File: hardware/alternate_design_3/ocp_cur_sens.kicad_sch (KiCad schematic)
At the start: 23 parts, among them U2 INA181, U3 INA181, U4 INA181, U8 LMV321, U9 TL331

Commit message: updates to kicad schema
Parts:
- added R4: R, symbol Device:R
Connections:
- net SD_A: now also R4.2
- net SENS_A: now also U9.1 (-), R4.1
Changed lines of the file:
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@@
+	)
+	(junction
+		(at 228.6 101.6)
+		(diameter 0)
+		(color 0 0 0 0)
 	)
 	(junction
@@
 		(color 0 0 0 0)
 	)
+	(junction
+		(at 205.74 104.14)
+		(diameter 0)
+		(color 0 0 0 0)
+	)
 	(wire
 		(pts
@@
 	(wire
 		(pts
+			(xy 205.74 104.14) (xy 205.74 124.46)
+		)
+		(stroke
+			(width 0)
+			(type default)
+		)
+	)
+	(wire
+		(pts
 			(xy 25.4 129.54) (xy 29.21 129.54)
 		)
@@
 	(wire
 		(pts
+			(xy 228.6 101.6) (xy 228.6 124.46)
+		)
+		(stroke
+			(width 0)
+			(type default)
+		)
+	)
+	(wire
+		(pts
 			(xy 34.29 182.88) (xy 34.29 185.42)
 		)
@@
 	(wire
 		(pts
+			(xy 198.12 104.14) (xy 205.74 104.14)
+		)
+		(stroke
+			(width 0)
+			(type default)
+		)
+	)
+	(wire
+		(pts
 			(xy 34.29 69.85) (xy 34.29 81.28)
 		)
@@
 	(wire
 		(pts
+			(xy 228.6 101.6) (xy 238.76 101.6)
+		)
+		(stroke
+			(width 0)
+			(type default)
+		)
+	)
+	(wire
+		(pts
 			(xy 59.69 165.1) (xy 59.69 163.83)
 		)
@@
 	(wire
 		(pts
+			(xy 205.74 104.14) (xy 210.82 104.14)
+		)
+		(stroke
+			(width 0)
+			(type default)
+		)
+	)
+	(wire
+		(pts
 			(xy 125.73 168.91) (xy 125.73 161.29)
 		)
@@
 	(wire
 		(pts
-			(xy 226.06 101.6) (xy 238.76 101.6)
+			(xy 226.06 101.6) (xy 228.6 101.6)
+		)
+		(stroke
+			(width 0)
+			(type default)
+		)
+	)
+	(wire
+		(pts
+			(xy 205.74 124.46) (xy 212.09 124.46)
 		)
 		(stroke
@@
 		(pts
 			(xy 198.12 99.06) (xy 210.82 99.06)
+		)
+		(stroke
+			(width 0)
+			(type default)
+		)
+	)
+	(wire
+		(pts
+			(xy 219.71 124.46) (xy 228.6 124.46)
 		)
 		(stroke
@@
 			)
 			(justify left bottom)
+		)
+	)
+	(label "VSHUNT_A"
+		(at 198.12 104.14 180)
+		(effects
+			(font
+				(size 1.27 1.27)
+			)
+			(justify right bottom)
 		)
 	)
@@
 	)
 	(symbol
+		(lib_id "Device:R")
+		(at 215.9 124.46 90)
+		(unit 1)
+		(body_style 1)
+		(exclude_from_sim no)
+		(in_bom yes)
+		(on_board yes)
+		(in_pos_files yes)
+		(dnp no)
+		(property "Reference" "R4"
+			(at 215.9 122.174 90)
+			(show_name no)
+			(do_not_autoplace no)
+			(effects
+				(font
+					(size 1.27 1.27)
+				)
+			)
+		)
+		(property "Value" "R"
+			(at 215.9 127.254 90)
+			(show_name no)
+			(do_not_autoplace no)
+			(effects
+				(font
+					(size 1.27 1.27)
+				)
+			)
+		)
+		(property "Footprint" ""
+			(at 215.9 126.238 90)
+			(hide yes)
+			(show_name no)
+			(do_not_autoplace no)
+			(effects
+				(font
+					(size 1.27 1.27)
+				)
+			)
+		)
+		(property "Datasheet" ""
+			(at 215.9 124.46 0)
+			(hide yes)
+			(show_name no)
+			(do_not_autoplace no)
+			(effects
+				(font
+					(size 1.27 1.27)
+				)
+			)
+		)
+		(property "Description" "Resistor"
+			(at 215.9 124.46 0)
+			(hide yes)
+			(show_name no)
+			(do_not_autoplace no)
+			(effects
+				(font
+					(size 1.27 1.27)
+				)
+			)
+		)
+		(pin "1"
+		)
+		(pin "2"
+		)
+		(instances
+			(project "mosfets"
+				(path "/6b82a8a8-ae2c-4987-9dc0-17eac5149d3f/902fe731-fd21-46ba-b7ee-b1d6cec2ca3c"
+					(reference "R4")
+					(unit 1)
+				)
+			)
+		)
+	)
+	(symbol
 		(lib_id "power:GNDA")
 		(at 34.29 185.42 0)
@@
 		(in_pos_files yes)
 		(dnp no)
-		(fields_autoplaced yes)
 		(property "Reference" "#PWR047"
 			(at 215.9 120.65 0)
@@
 		)
 		(property "Value" "GNDA"
-			(at 215.9 119.38 0)
-			(show_name no)
-			(do_not_autoplace no)
+			(at 215.9 118.364 0)
+			(show_name no)
+			(do_not_autoplace no)

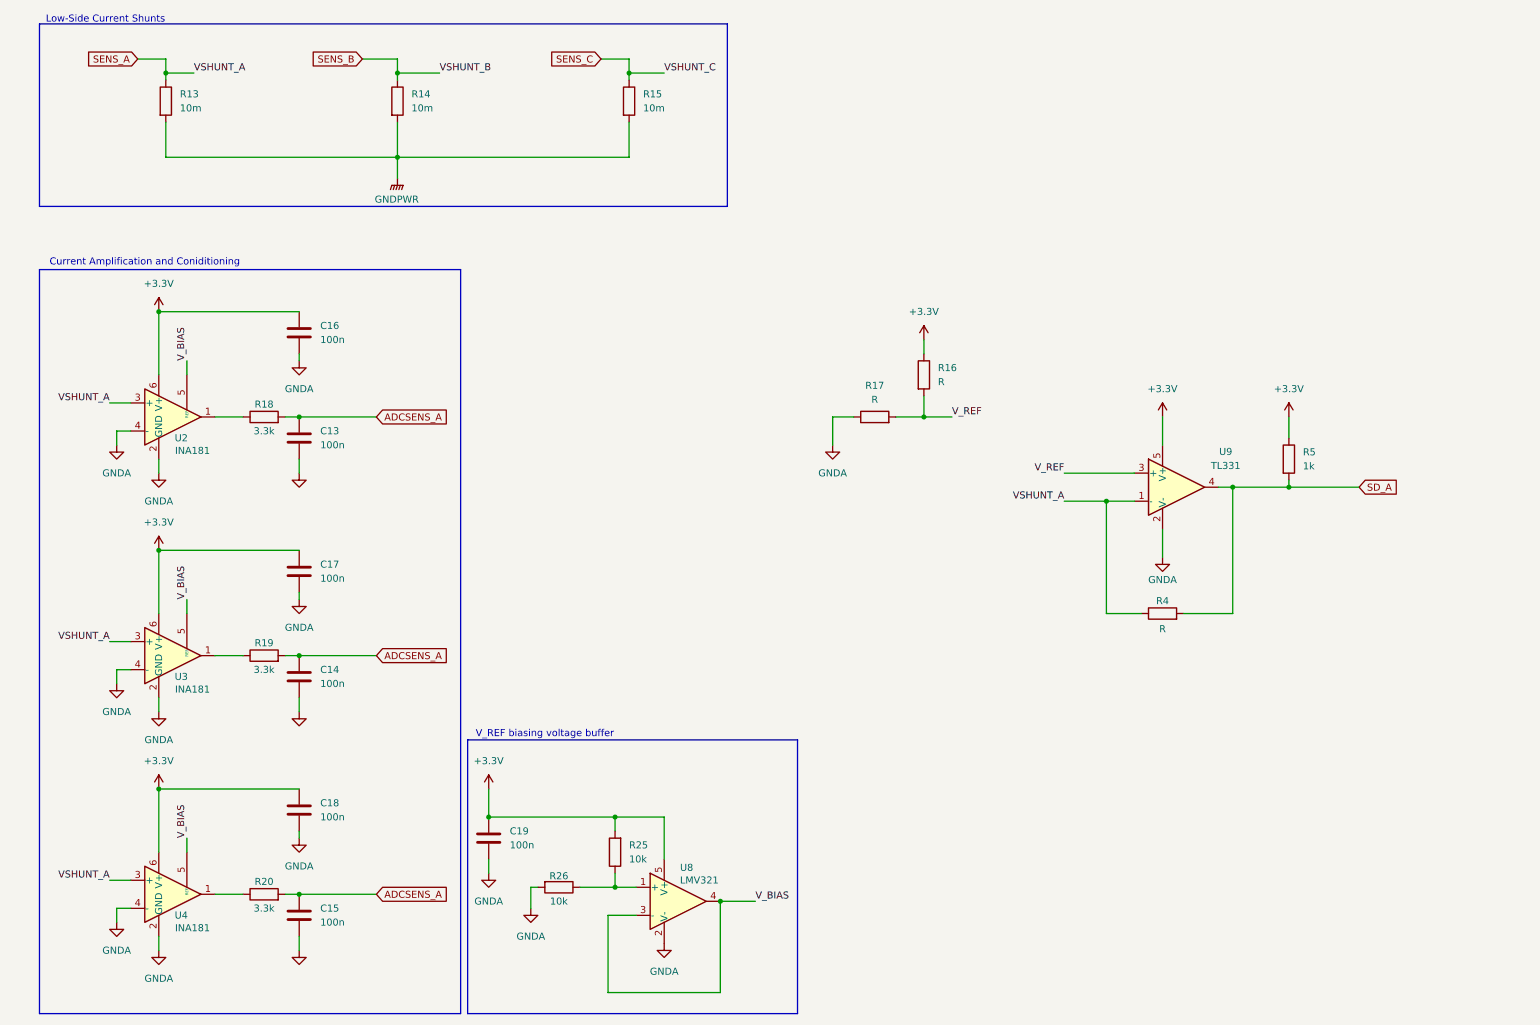
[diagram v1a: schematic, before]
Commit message: added OCP
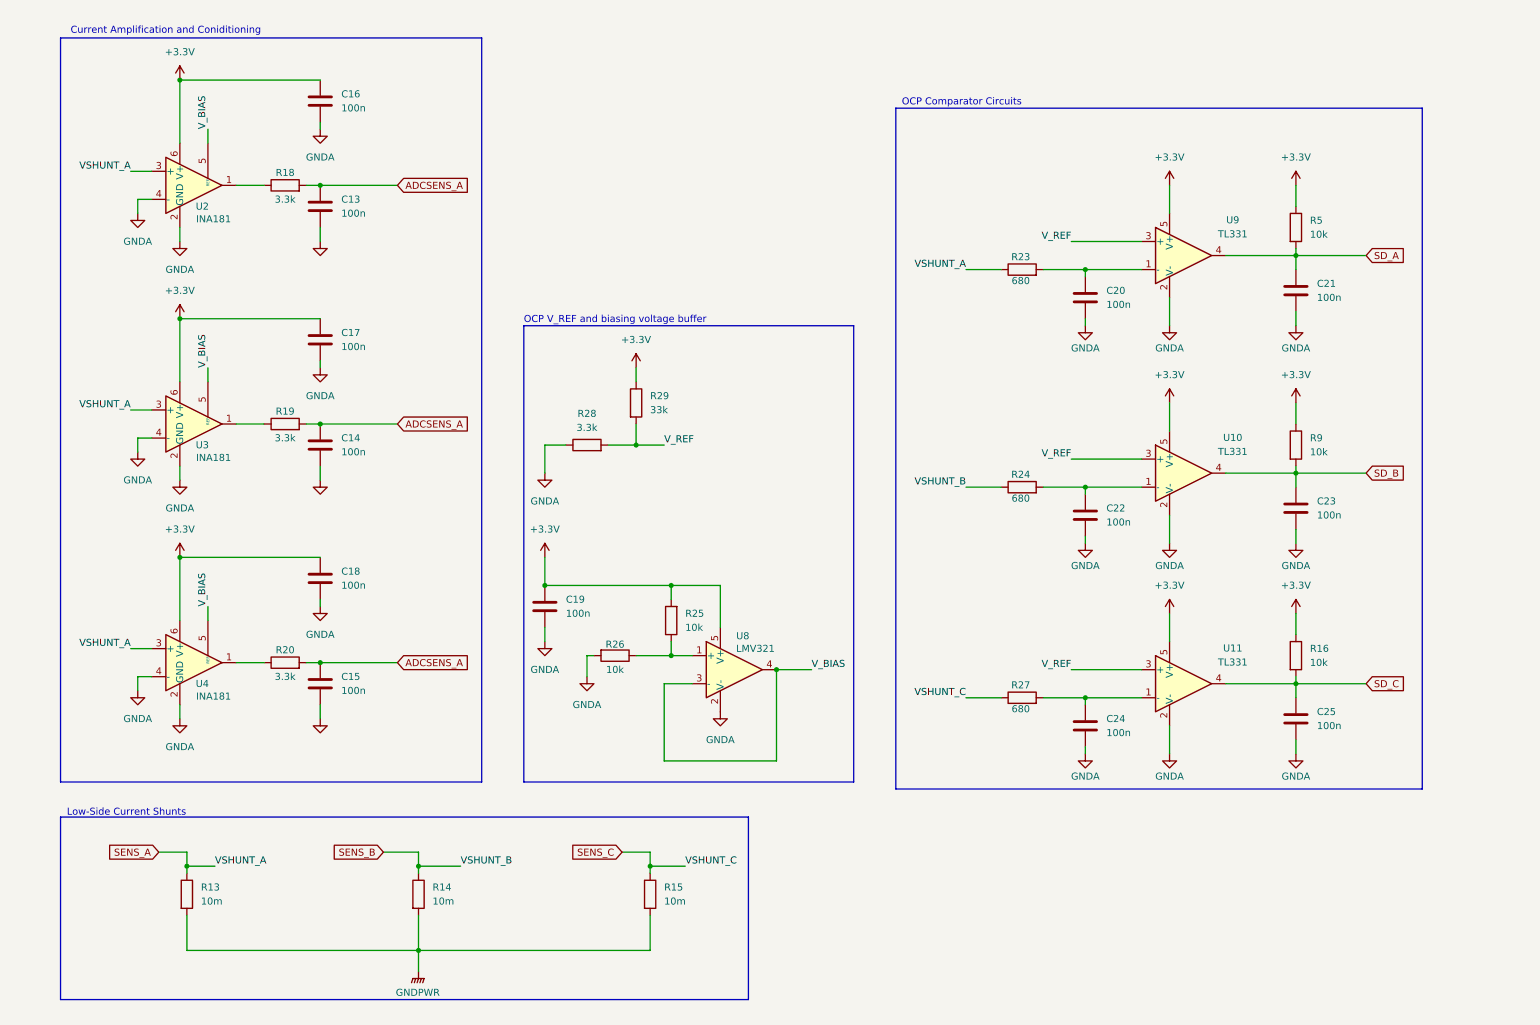
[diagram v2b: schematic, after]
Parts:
- removed R17, R4: R, symbol Device:R
- added C20, C21, C22, C23, C24, C25: 100n, symbol Device:C
- added R23, R24, R27: 680, symbol Device:R
- added R28: 3.3k, symbol Device:R
- added R29: 33k, symbol Device:R
- added R9: 10k, symbol Device:R
- added U10, U11: TL331, Package_TO_SOT_SMD:SOT-23-5, symbol Comparator:TL331
- R16: value R -> 10k
- R5: value 1k -> 10k
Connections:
- net +3.3V: now also R29.1, R9.1, U10.5 (V+), U11.5 (V+)
- net GNDA: now also C20.2, C21.2, C22.2, C23.2, C24.2, C25.2, R28.1, U10.2 (V-), U11.2 (V-)
- net SD_A: now also C21.1
- net SENS_A: now also R23.1; no longer U9.1 (-)
- net SENS_B: now also R24.1
- net SENS_C: now also R27.1
- net V_REF: now also R28.2, R29.2, U10.3 (+), U11.3 (+); no longer R16.2
- new net: C22.1, R24.2, U10.1 (-)
- new net: C20.1, R23.2, U9.1 (-)
- new net: C24.1, R27.2, U11.1 (-)
- new net SD_B: C23.1, R9.2, U10.4
- new net SD_C: C25.1, R16.2, U11.4
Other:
- note added: "OCP Comparator Circuits"
- note added: "OCP V_REF and biasing voltage buffer"
- note removed: "V_REF biasing voltage buffer"
- moved on the sheet: C13, C14, C15, C16, C17, C18, C19, R13, R14, R15, R18, R19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

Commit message: major additions to schematic of inverter
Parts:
- added TP13, TP14, TP15, TP16, TP17, TP18, TP20, TP24: TestPoint, symbol Connector:TestPoint
- added U13: 74LVC1G11, symbol 74xGxx:74LVC1G11
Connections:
- net +3.3V: now also U13.5 (VCC)
- net GNDA: no longer U2.4 (-), U3.4 (-), U4.4 (-)
- net GNDPWR: now also U2.4 (-), U3.4 (-), U4.4 (-)
- net SD_A: now also TP18.1, U13.6
- net SD_B: now also TP24.1, U13.1
- net SD_C: now also TP20.1, U13.3
- net SENS_A: no longer U3.3 (+), U4.3 (+)
- net SENS_B: now also U3.3 (+)
- net SENS_C: now also U4.3 (+)
- net V_BIAS: now also TP17.1
- net V_REF: now also TP16.1
- removed net ADCSENS_A: C13.1, C14.1, C15.1, R18.2, R19.2, R20.2
- new net ADC_SENS_A: C13.1, R18.2, TP13.1
- new net ADC_SENS_B: C14.1, R19.2, TP14.1
- new net ADC_SENS_C: C15.1, R20.2, TP15.1
- new net BRK_IN: U13.4
- new net GNDD: U13.2 (GND)
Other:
- note added: "MCU SHUTDOWN"
- moved on the sheet: C19, C20, C21, C22, C23, C24, C25, R13, R14, R15, R16, R23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
